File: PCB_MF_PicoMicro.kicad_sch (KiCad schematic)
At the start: 8 parts, among them J1 Conn_01x12, J2 Conn_01x12, J7 Conn_01x02_Pin, J8 Conn_01x02_Pin

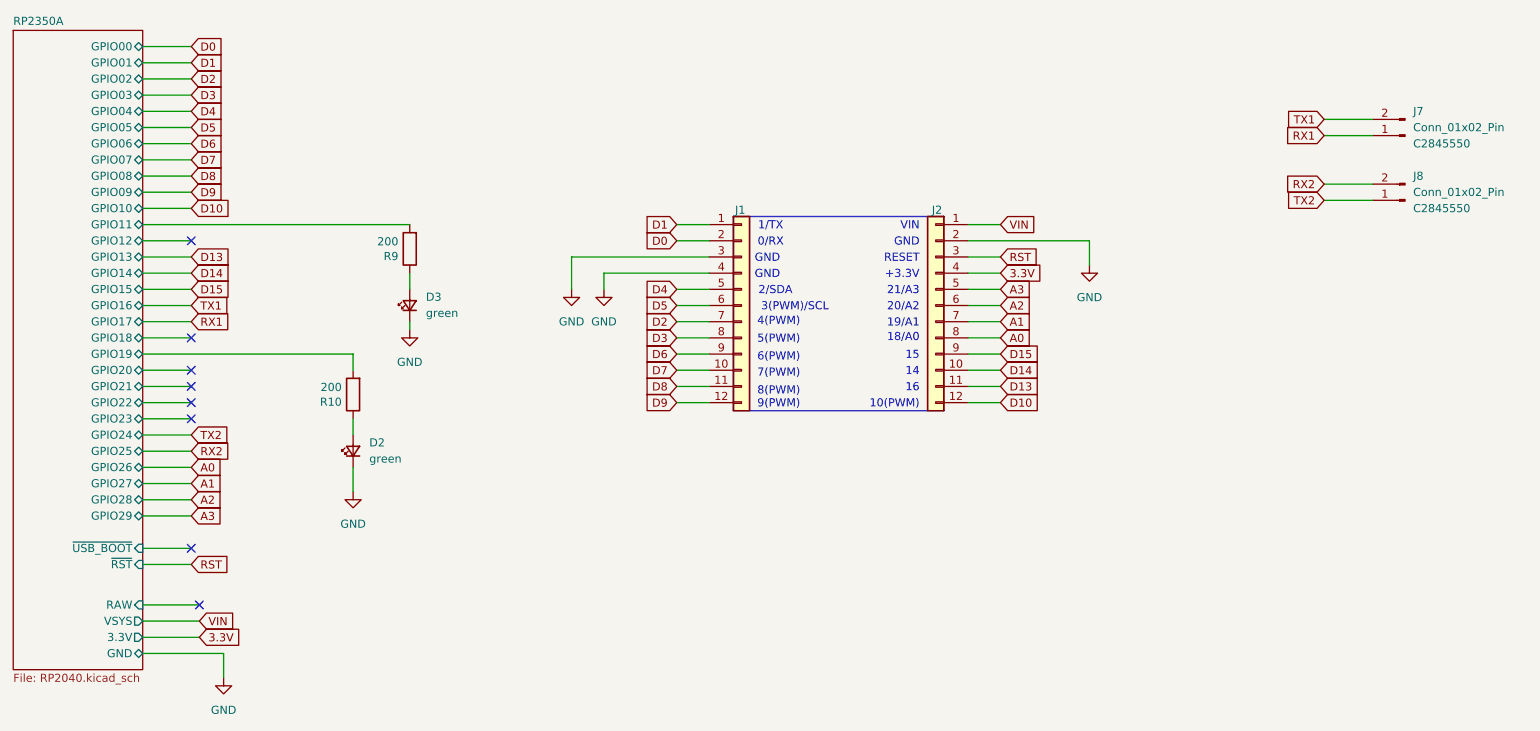
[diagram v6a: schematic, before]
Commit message: change ProMicro footprint to standard connector
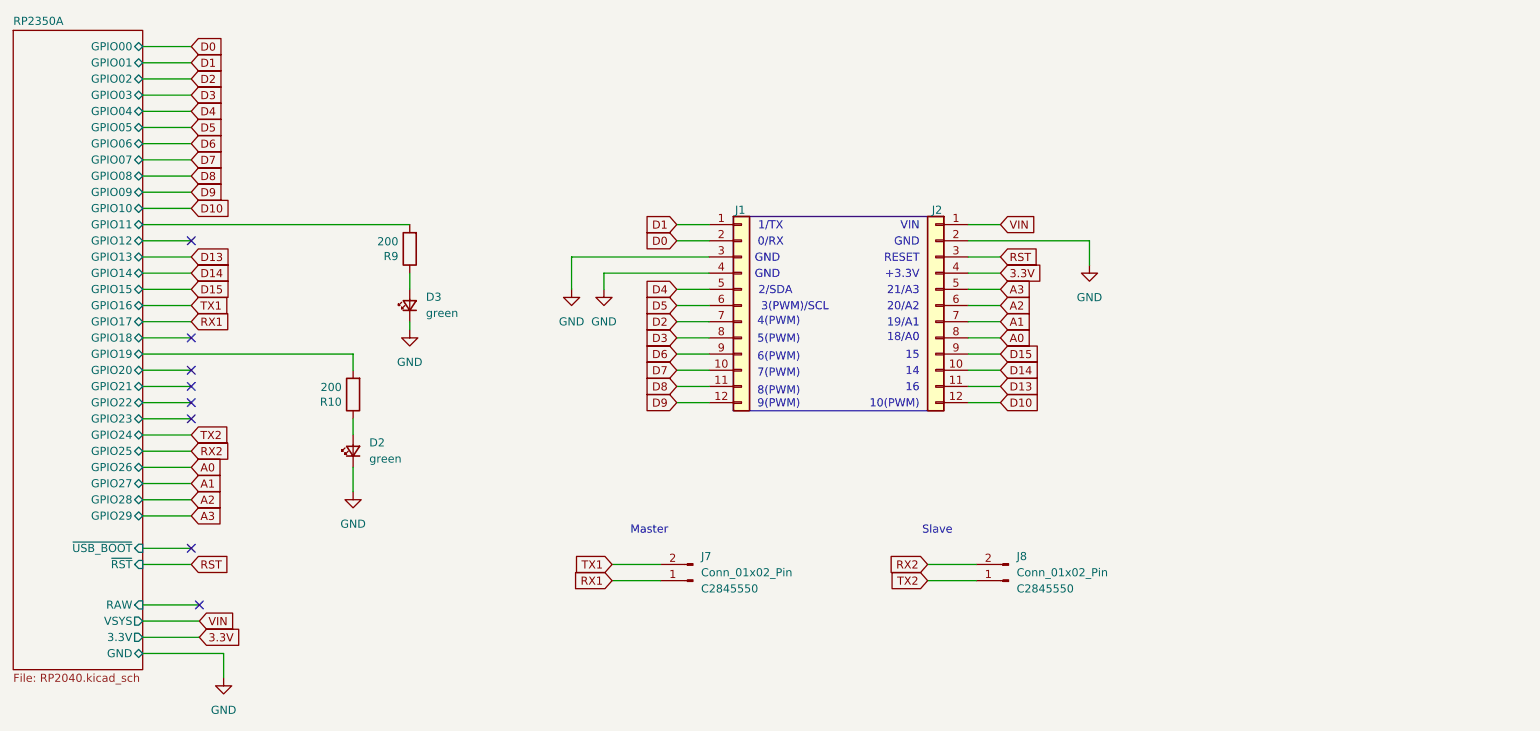
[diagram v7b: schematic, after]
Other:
- note added: "Master"
- note added: "Slave"
- moved on the sheet: J7, J8
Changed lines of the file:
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@@
+		)
+	)
+	(text "Slave"
+		(exclude_from_sim no)
+		(at 172.974 112.776 0)
+		(effects
+			(font
+				(size 1.27 1.27)
+			)
 		)
 	)
@@
 		(exclude_from_sim no)
 		(at 146.304 70.104 0)
+		(effects
+			(font
+				(size 1.27 1.27)
+			)
+		)
+	)
+	(text "Master"
+		(exclude_from_sim no)
+		(at 127.762 112.776 0)
 		(effects
 			(font
@@
 	(wire
 		(pts
-			(xy 233.68 58.42) (xy 241.3 58.42)
+			(xy 171.45 118.11) (xy 179.07 118.11)
 		)
 		(stroke
@@
 	(wire
 		(pts
-			(xy 233.68 48.26) (xy 241.3 48.26)
+			(xy 121.92 118.11) (xy 129.54 118.11)
 		)
 		(stroke
@@
 	(wire
 		(pts
-			(xy 233.68 60.96) (xy 241.3 60.96)
+			(xy 171.45 120.65) (xy 179.07 120.65)
 		)
 		(stroke
@@
 	(wire
 		(pts
-			(xy 233.68 50.8) (xy 241.3 50.8)
+			(xy 121.92 120.65) (xy 129.54 120.65)
 		)
 		(stroke
@@
 	(global_label "RX1"
 		(shape input)
-		(at 233.68 50.8 180)
-		(fields_autoplaced yes)
-		(effects
-			(font
-				(size 1.27 1.27)
-			)
-			(justify right)
-		)
-		(property "Intersheetrefs" "${INTERSHEET_REFS}"
-			(at 227.0058 50.8 0)
+		(at 121.92 120.65 180)
+		(fields_autoplaced yes)
+		(effects
+			(font
+				(size 1.27 1.27)
+			)
+			(justify right)
+		)
+		(property "Intersheetrefs" "${INTERSHEET_REFS}"
+			(at 115.2458 120.65 0)
 			(effects
 				(font
@@
 	(global_label "TX1"
 		(shape input)
-		(at 233.68 48.26 180)
-		(fields_autoplaced yes)
-		(effects
-			(font
-				(size 1.27 1.27)
-			)
-			(justify right)
-		)
-		(property "Intersheetrefs" "${INTERSHEET_REFS}"
-			(at 227.3082 48.26 0)
+		(at 121.92 118.11 180)
+		(fields_autoplaced yes)
+		(effects
+			(font
+				(size 1.27 1.27)
+			)
+			(justify right)
+		)
+		(property "Intersheetrefs" "${INTERSHEET_REFS}"
+			(at 115.5482 118.11 0)
 			(effects
 				(font
@@
 	(global_label "RX2"
 		(shape input)
-		(at 233.68 58.42 180)
-		(fields_autoplaced yes)
-		(effects
-			(font
-				(size 1.27 1.27)
-			)
-			(justify right)
-		)
-		(property "Intersheetrefs" "${INTERSHEET_REFS}"
-			(at 227.0058 58.42 0)
+		(at 171.45 118.11 180)
+		(fields_autoplaced yes)
+		(effects
+			(font
+				(size 1.27 1.27)
+			)
+			(justify right)
+		)
+		(property "Intersheetrefs" "${INTERSHEET_REFS}"
+			(at 164.7758 118.11 0)
 			(effects
 				(font
@@
 	(global_label "TX2"
 		(shape input)
-		(at 233.68 60.96 180)
-		(fields_autoplaced yes)
-		(effects
-			(font
-				(size 1.27 1.27)
-			)
-			(justify right)
-		)
-		(property "Intersheetrefs" "${INTERSHEET_REFS}"
-			(at 227.3082 60.96 0)
+		(at 171.45 120.65 180)
+		(fields_autoplaced yes)
+		(effects
+			(font
+				(size 1.27 1.27)
+			)
+			(justify right)
+		)
+		(property "Intersheetrefs" "${INTERSHEET_REFS}"
+			(at 165.0782 120.65 0)
 			(effects
 				(font
@@
 	(symbol
 		(lib_id "_Own_Library:Conn_01x02_JST_ZH")
-		(at 246.38 50.8 180)
+		(at 134.62 120.65 180)
 		(unit 1)
 		(exclude_from_sim no)
@@
 		(fields_autoplaced yes)
 		(property "Reference" "J7"
-			(at 247.65 46.9899 0)
+			(at 135.89 116.8399 0)
 			(effects
 				(font
@@
 		)
 		(property "Value" "Conn_01x02_Pin"
-			(at 247.65 49.5299 0)
+			(at 135.89 119.3799 0)
 			(effects
 				(font
@@
 		)
 		(property "Footprint" "_Own_Library:JST_ZH_B2B-ZR_1x02_P1.50mm_Vertical"
-			(at 246.38 50.8 0)
+			(at 134.62 120.65 0)
 			(effects
 				(font
@@
 		)
 		(property "Datasheet" "~"
-			(at 246.38 50.8 0)
+			(at 134.62 120.65 0)
 			(effects
 				(font
@@
 		)
 		(property "Description" "Generic connector, single row, 01x02, script generated"
-			(at 246.38 50.8 0)
+			(at 134.62 120.65 0)
 			(effects
 				(font
@@
 		)
 		(property "JLCPCB" "C2845550"
-			(at 247.65 52.0699 0)
+			(at 135.89 121.9199 0)
 			(effects
 				(font
@@
 	(symbol
 		(lib_id "_Own_Library:Conn_01x02_JST_ZH")
-		(at 246.38 60.96 180)
+		(at 184.15 120.65 180)
 		(unit 1)
 		(exclude_from_sim no)
@@
 		(fields_autoplaced yes)
 		(property "Reference" "J8"
-			(at 247.65 57.1499 0)
+			(at 185.42 116.8399 0)
 			(effects
 				(font
@@
 		)
 		(property "Value" "Conn_01x02_Pin"
-			(at 247.65 59.6899 0)
+			(at 185.42 119.3799 0)
 			(effects
 				(font
@@
 		)
 		(property "Footprint" "_Own_Library:JST_ZH_B2B-ZR_1x02_P1.50mm_Vertical"
-			(at 246.38 60.96 0)
+			(at 184.15 120.65 0)
 			(effects
 				(font
@@
 		)
 		(property "Datasheet" "~"
-			(at 246.38 60.96 0)
+			(at 184.15 120.65 0)
 			(effects
 				(font
@@
 		)
 		(property "Description" "Generic connector, single row, 01x02, script generated"
-			(at 246.38 60.96 0)
+			(at 184.15 120.65 0)
 			(effects
 				(font
@@
 		)
 		(property "JLCPCB" "C2845550"
-			(at 247.65 62.2299 0)
-			(effects
-				(font
+			(at 185.42 121.9199 0)
+			(effects
+				(font

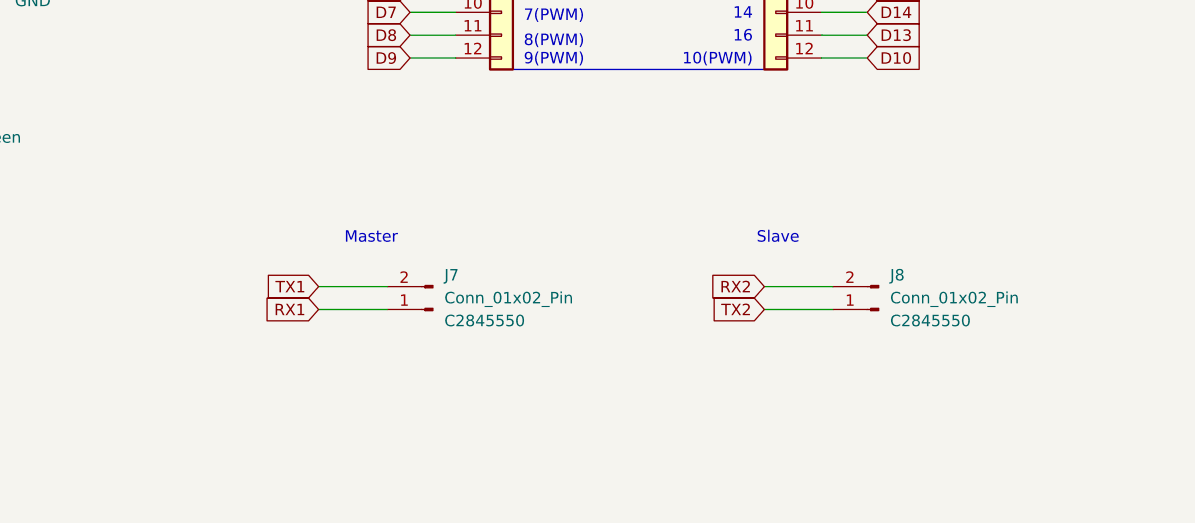
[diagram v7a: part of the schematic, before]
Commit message: serial resistor for TX line
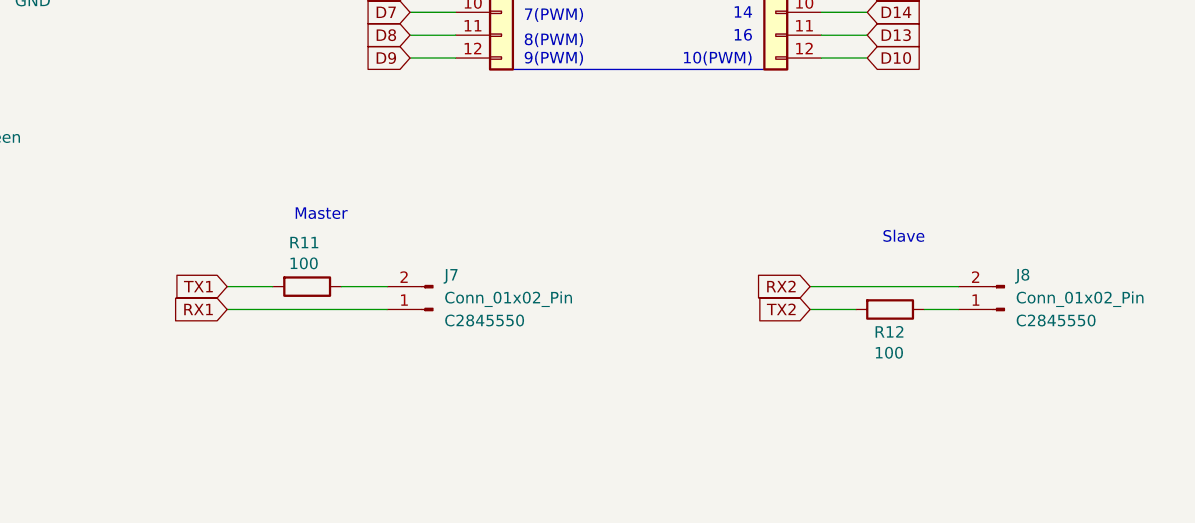
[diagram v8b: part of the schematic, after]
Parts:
- added R11, R12: 100, Resistor_SMD:R_0402_1005Metric, symbol Device:R
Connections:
- net TX1: now also R11.2; no longer J7.2 (Pin_2)
- net TX2: now also R12.2; no longer J8.1 (Pin_1)
- new net: J7.2 (Pin_2), R11.1
- new net: J8.1 (Pin_1), R12.1
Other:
- moved on the sheet: J8
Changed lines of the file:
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@@
 	(text "Slave"
 		(exclude_from_sim no)
-		(at 172.974 112.776 0)
+		(at 186.944 112.776 0)
 		(effects
 			(font
@@
 	(text "Master"
 		(exclude_from_sim no)
-		(at 127.762 112.776 0)
+		(at 122.174 110.236 0)
 		(effects
 			(font
@@
 	(wire
 		(pts
+			(xy 176.53 118.11) (xy 193.04 118.11)
+		)
+		(stroke
+			(width 0)
+			(type default)
+		)
+	)
+	(wire
+		(pts
 			(xy 48.26 100.33) (xy 55.88 100.33)
 		)
@@
 	(wire
 		(pts
+			(xy 111.76 118.11) (xy 116.84 118.11)
+		)
+		(stroke
+			(width 0)
+			(type default)
+		)
+	)
+	(wire
+		(pts
 			(xy 81.28 102.87) (xy 81.28 106.68)
 		)
@@
 	(wire
 		(pts
-			(xy 171.45 118.11) (xy 179.07 118.11)
-		)
-		(stroke
-			(width 0)
-			(type default)
-		)
-	)
-	(wire
-		(pts
 			(xy 132.08 90.17) (xy 137.16 90.17)
 		)
@@
 	(wire
 		(pts
+			(xy 189.23 120.65) (xy 193.04 120.65)
+		)
+		(stroke
+			(width 0)
+			(type default)
+		)
+	)
+	(wire
+		(pts
 			(xy 120.65 72.39) (xy 120.65 74.93)
 		)
@@
 	(wire
 		(pts
+			(xy 124.46 118.11) (xy 129.54 118.11)
+		)
+		(stroke
+			(width 0)
+			(type default)
+		)
+	)
+	(wire
+		(pts
 			(xy 48.26 110.49) (xy 55.88 110.49)
 		)
@@
 	(wire
 		(pts
-			(xy 121.92 118.11) (xy 129.54 118.11)
-		)
-		(stroke
-			(width 0)
-			(type default)
-		)
-	)
-	(wire
-		(pts
 			(xy 132.08 82.55) (xy 137.16 82.55)
 		)
@@
 	(wire
 		(pts
+			(xy 176.53 120.65) (xy 181.61 120.65)
+		)
+		(stroke
+			(width 0)
+			(type default)
+		)
+	)
+	(wire
+		(pts
 			(xy 48.26 115.57) (xy 55.88 115.57)
 		)
@@
 	(wire
 		(pts
-			(xy 171.45 120.65) (xy 179.07 120.65)
-		)
-		(stroke
-			(width 0)
-			(type default)
-		)
-	)
-	(wire
-		(pts
 			(xy 132.08 74.93) (xy 137.16 74.93)
 		)
@@
 	(wire
 		(pts
-			(xy 121.92 120.65) (xy 129.54 120.65)
+			(xy 111.76 120.65) (xy 129.54 120.65)
 		)
 		(stroke
@@
 	(global_label "RX1"
 		(shape input)
-		(at 121.92 120.65 180)
+		(at 111.76 120.65 180)
 		(fields_autoplaced yes)
 		(effects
@@
 		)
 		(property "Intersheetrefs" "${INTERSHEET_REFS}"
-			(at 115.2458 120.65 0)
+			(at 105.0858 120.65 0)
 			(effects
 				(font
@@
 	(global_label "TX1"
 		(shape input)
-		(at 121.92 118.11 180)
+		(at 111.76 118.11 180)
 		(fields_autoplaced yes)
 		(effects
@@
 		)
 		(property "Intersheetrefs" "${INTERSHEET_REFS}"
-			(at 115.5482 118.11 0)
+			(at 105.3882 118.11 0)
 			(effects
 				(font
@@
 	(global_label "RX2"
 		(shape input)
-		(at 171.45 118.11 180)
+		(at 176.53 118.11 180)
 		(fields_autoplaced yes)
 		(effects
@@
 		)
 		(property "Intersheetrefs" "${INTERSHEET_REFS}"
-			(at 164.7758 118.11 0)
+			(at 169.8558 118.11 0)
 			(effects
 				(font
@@
 	(global_label "TX2"
 		(shape input)
-		(at 171.45 120.65 180)
+		(at 176.53 120.65 180)
 		(fields_autoplaced yes)
 		(effects
@@
 		)
 		(property "Intersheetrefs" "${INTERSHEET_REFS}"
-			(at 165.0782 120.65 0)
+			(at 170.1582 120.65 0)
 			(effects
 				(font
@@
 	(symbol
 		(lib_id "_Own_Library:Conn_01x02_JST_ZH")
-		(at 184.15 120.65 180)
+		(at 198.12 120.65 180)
 		(unit 1)
 		(exclude_from_sim no)
@@
 		(fields_autoplaced yes)
 		(property "Reference" "J8"
-			(at 185.42 116.8399 0)
+			(at 199.39 116.8399 0)
 			(effects
 				(font
@@
 		)
 		(property "Value" "Conn_01x02_Pin"
-			(at 185.42 119.3799 0)
+			(at 199.39 119.3799 0)
 			(effects
 				(font
@@
 		)
 		(property "Footprint" "_Own_Library:JST_ZH_B2B-ZR_1x02_P1.50mm_Vertical"
-			(at 184.15 120.65 0)
+			(at 198.12 120.65 0)
 			(effects
 				(font
@@
 		)
 		(property "Datasheet" "~"
-			(at 184.15 120.65 0)
+			(at 198.12 120.65 0)
 			(effects
 				(font
@@
 		)
 		(property "Description" "Generic connector, single row, 01x02, script generated"
-			(at 184.15 120.65 0)
+			(at 198.12 120.65 0)
 			(effects
 				(font
@@
 		)
 		(property "JLCPCB" "C2845550"
-			(at 185.42 121.9199 0)
+			(at 199.39 121.9199 0)
 			(effects
 				(font
@@
 	)
 	(symbol
+		(lib_id "Device:R")
+		(at 120.65 118.11 270)
+		(unit 1)
+		(exclude_from_sim no)
+		(in_bom yes)
+		(on_board yes)
+		(dnp no)
+		(property "Reference" "R11"
+			(at 118.618 113.2586 90)
+			(effects
+				(font
+					(size 1.27 1.27)
+				)
+				(justify left)
+			)
+		)
+		(property "Value" "100"
+			(at 118.618 115.57 90)
+			(effects
+				(font
+					(size 1.27 1.27)
+				)
+				(justify left)
+			)
+		)
+		(property "Footprint" "Resistor_SMD:R_0402_1005Metric"
+			(at 120.65 116.332 90)
+			(effects
+				(font
+					(size 1.27 1.27)
+				)
+				(hide yes)
+			)
+		)
+		(property "Datasheet" "~"
+			(at 120.65 118.11 0)
+			(effects
+				(font
+					(size 1.27 1.27)
+				)
+				(hide yes)
+			)
+		)
+		(property "Description" ""
+			(at 120.65 118.11 0)
+			(effects
+				(font
+					(size 1.27 1.27)
+				)
+			)
+		)
+		(pin "1"
+		)
+		(pin "2"
+		)
+		(instances
+			(project "PCB_MF_PicoMicro"
+				(path "/e63e39d7-6ac0-4ffd-8aa3-1841a4541b55"
+					(reference "R11")
+					(unit 1)
+				)
+			)
+		)
+	)
+	(symbol
 		(lib_id "power:GND")
 		(at 120.65 74.93 0)
@@
 					(unit 1)
 				)
+			)
+		)
+	)
+	(symbol
+		(lib_id "Device:R")
+		(at 185.42 120.65 270)
+		(unit 1)
+		(exclude_from_sim no)
+		(in_bom yes)
+		(on_board yes)
+		(dnp no)
+		(property "Reference" "R12"
+			(at 183.642 123.19 90)
+			(effects
+				(font
+					(size 1.27 1.27)
+				)
+				(justify left)
+			)
+		)
+		(property "Value" "100"
+			(at 183.642 125.5014 90)
+			(effects
+				(font
+					(size 1.27 1.27)
+				)
+				(justify left)
+			)
+		)
+		(property "Footprint" "Resistor_SMD:R_0402_1005Metric"
+			(at 185.42 118.872 90)
+			(effects
+				(font
+					(size 1.27 1.27)
+				)
+				(hide yes)
+			)
+		)
+		(property "Datasheet" "~"
+			(at 185.42 120.65 0)
+			(effects
+				(font
+					(size 1.27 1.27)
+				)
+				(hide yes)
+			)
+		)
+		(property "Description" ""
+			(at 185.42 120.65 0)
+			(effects
+				(font
+					(size 1.27 1.27)
+				)
+			)
+		)
+		(pin "1"
+		)
+		(pin "2"
+		)
+		(instances
+			(project "PCB_MF_PicoMicro"
+				(path "/e63e39d7-6ac0-4ffd-8aa3-1841a4541b55"
+					(reference "R12")
+					(unit 1)
+				)
